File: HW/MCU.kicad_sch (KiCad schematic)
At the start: 7 parts, among them U6 STM32C031KxTx, U7 STM32C031KxUx

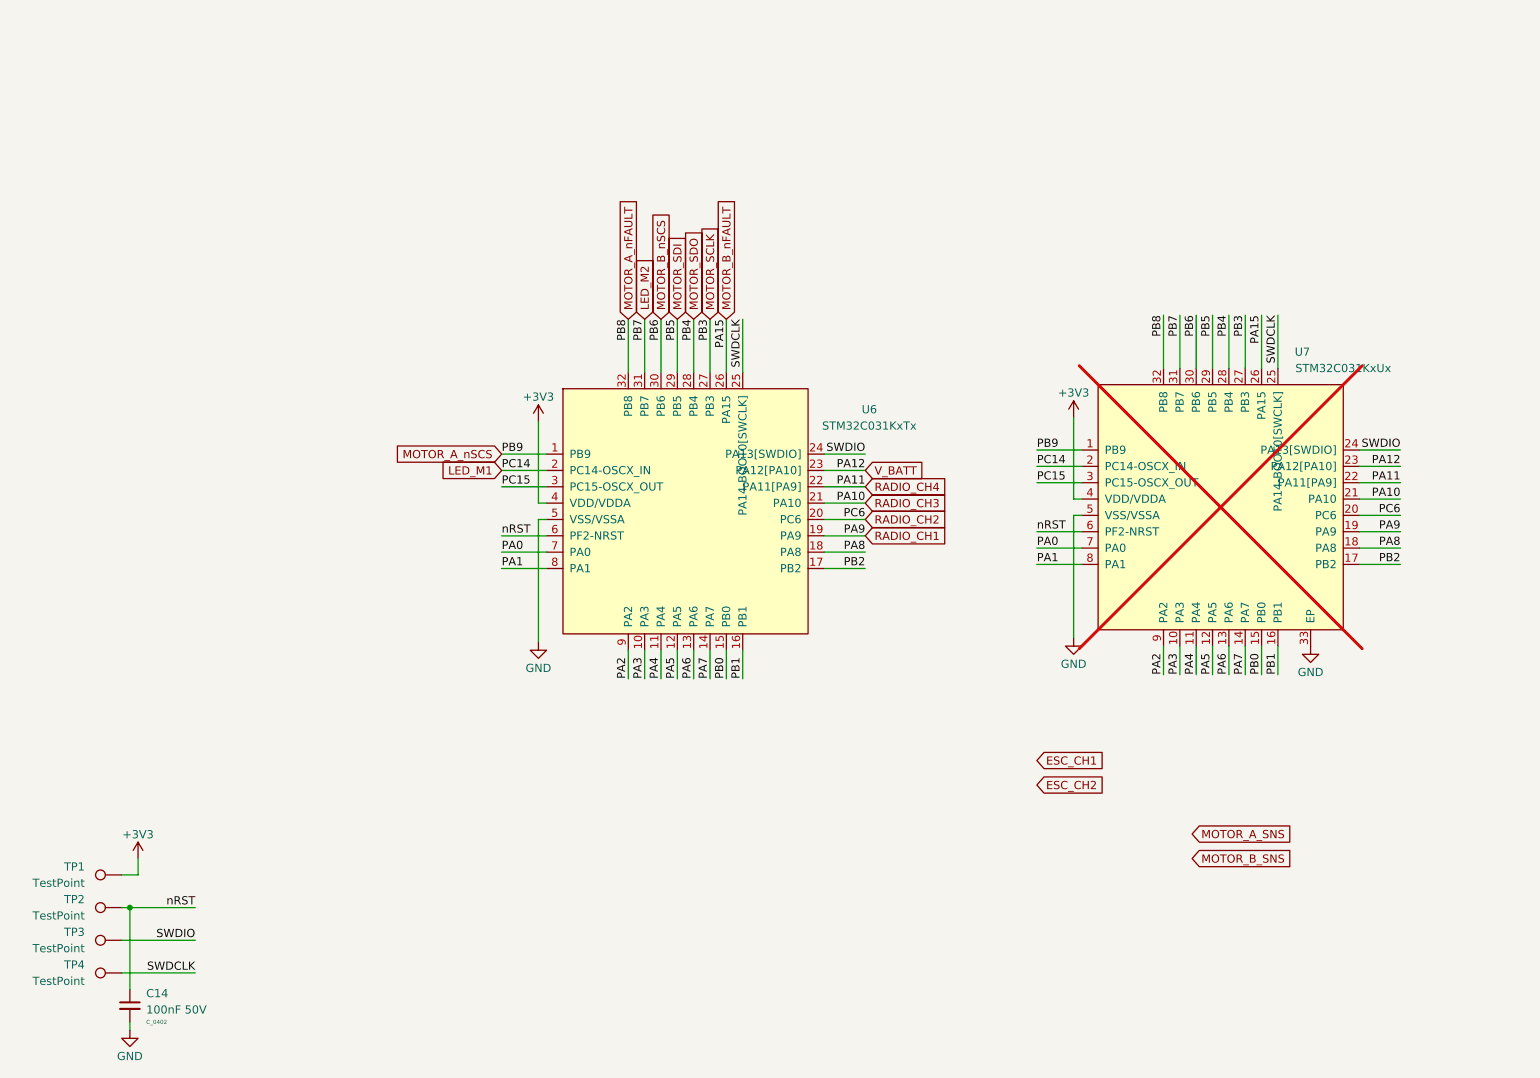
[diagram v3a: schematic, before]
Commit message: Move 5V Supply Around To Make More Efficient Conduction Path
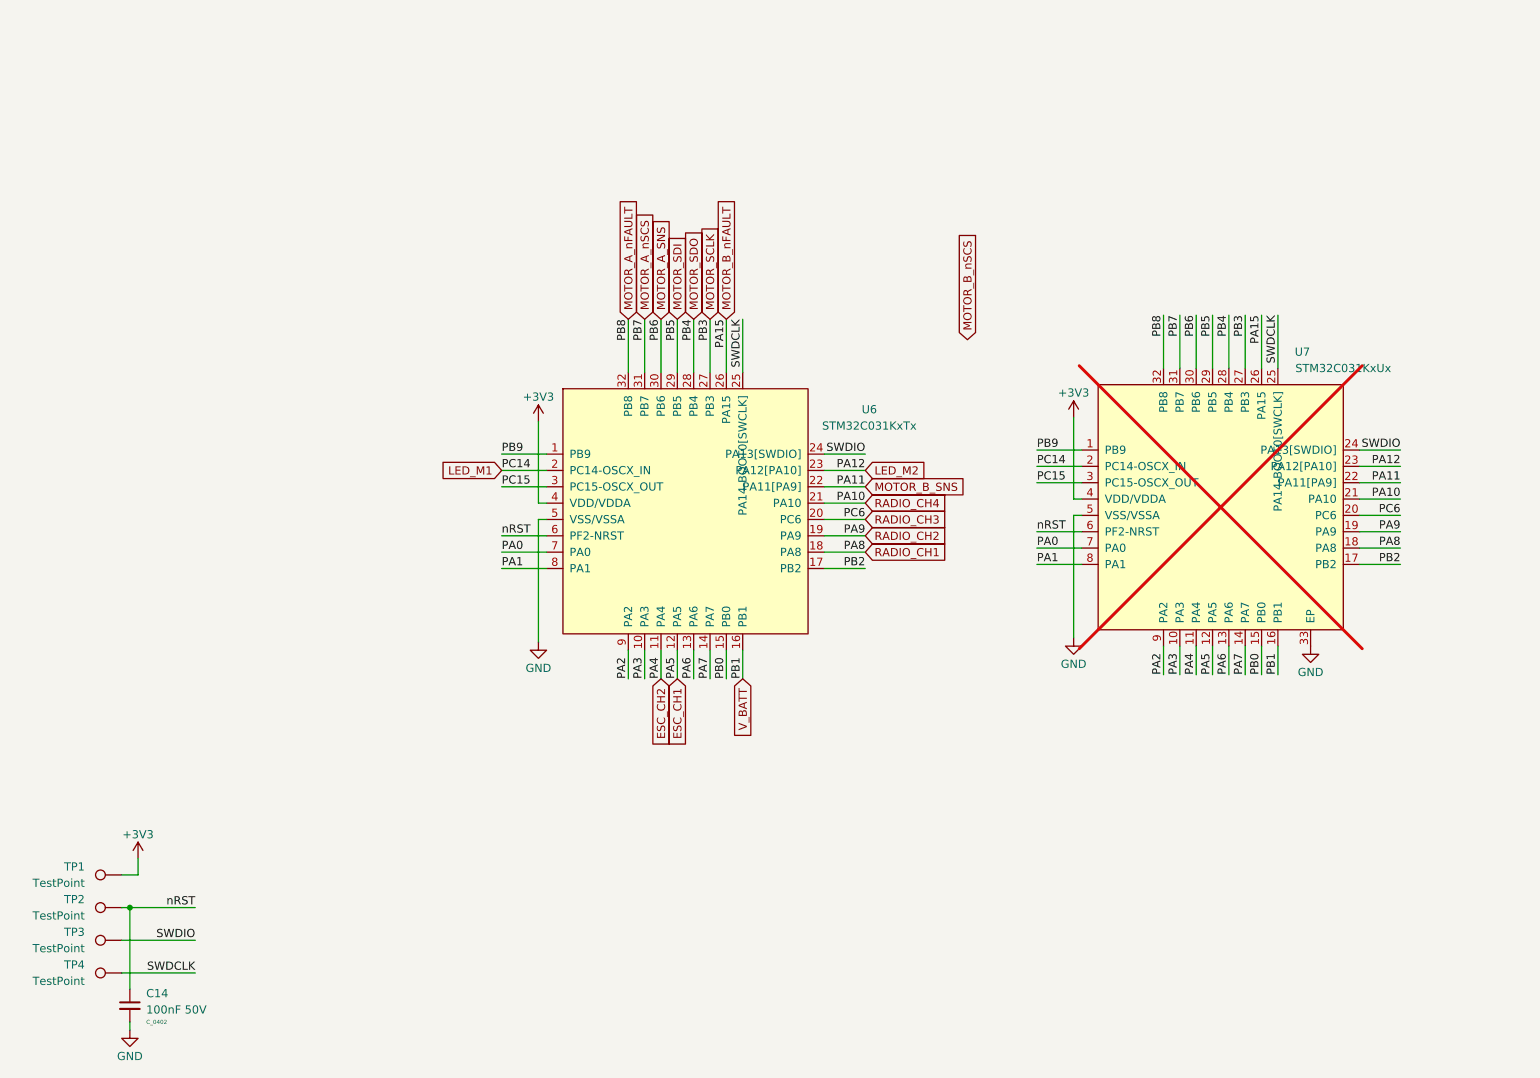
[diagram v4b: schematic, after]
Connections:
- net PA4 is gone; now on net ESC_CH2: U6.11 (PA4), U7.11 (PA4)
- net PA5 is gone; now on net ESC_CH1: U6.12 (PA5), U7.12 (PA5)
- net PA8 is gone; now on net RADIO_CH1: U6.18 (PA8), U7.18 (PA8)
- net PB1 is gone; now on net V_BATT: U6.16 (PB1), U7.16 (PB1)
- net LED_M2: now also U6.23 (PA12[PA10]), U7.23 (PA12[PA10]); no longer U6.31 (PB7), U7.31 (PB7)
- net MOTOR_A_SNS: now also U6.30 (PB6), U7.30 (PB6)
- net MOTOR_A_nSCS: now also U6.31 (PB7), U7.31 (PB7); no longer U6.1 (PB9), U7.1 (PB9)
- net MOTOR_B_SNS: now also U6.22 (PA11[PA9]), U7.22 (PA11[PA9])
- net MOTOR_B_nSCS: no longer U6.30 (PB6), U7.30 (PB6)
- net RADIO_CH1: no longer U6.19 (PA9), U7.19 (PA9)
- net RADIO_CH2: now also U6.19 (PA9), U7.19 (PA9); no longer U6.20 (PC6), U7.20 (PC6)
- net RADIO_CH3: now also U6.20 (PC6), U7.20 (PC6); no longer U6.21 (PA10), U7.21 (PA10)
- net RADIO_CH4: now also U6.21 (PA10), U7.21 (PA10); no longer U6.22 (PA11[PA9]), U7.22 (PA11[PA9])
- net V_BATT: no longer U6.23 (PA12[PA10]), U7.23 (PA12[PA10])
- new net PB9: U6.1 (PB9), U7.1 (PB9)
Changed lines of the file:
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@@
     (stroke (width 0) (type default))
   )
-  (wire (pts (xy 133.35 79.375) (xy 133.35 71.12))
+  (wire (pts (xy 133.35 71.12) (xy 133.35 79.375))
     (stroke (width 0) (type default))
   )
@@
     (effects (font (size 1.27 1.27)) (justify left bottom))
   )
-  (global_label "RADIO_CH2" (shape input) (at 167.64 102.235 0) (fields_autoplaced)
+  (global_label "V_BATT" (shape input) (at 148.59 127 270) (fields_autoplaced)
+    (effects (font (size 1.27 1.27)) (justify right))
+    (property "Intersheetrefs" "${INTERSHEET_REFS}" (at 148.59 136.3352 90)
+      (effects (font (size 1.27 1.27)) (justify right))
+    )
+  )
+  (global_label "MOTOR_A_SNS" (shape input) (at 135.89 71.12 90) (fields_autoplaced)
+    (effects (font (size 1.27 1.27)) (justify left))
+    (property "Intersheetrefs" "${INTERSHEET_REFS}" (at 135.89 55.0115 90)
+      (effects (font (size 1.27 1.27)) (justify left))
+    )
+  )
+  (global_label "RADIO_CH3" (shape input) (at 167.64 102.235 0) (fields_autoplaced)
     (effects (font (size 1.27 1.27)) (justify left))
     (property "Intersheetrefs" "${INTERSHEET_REFS}" (at 180.9667 102.235 0)
@@
     )
   )
-  (global_label "MOTOR_B_nSCS" (shape input) (at 135.89 71.12 90) (fields_autoplaced)
+  (global_label "ESC_CH2" (shape input) (at 135.89 127 270) (fields_autoplaced)
+    (effects (font (size 1.27 1.27)) (justify right))
+    (property "Intersheetrefs" "${INTERSHEET_REFS}" (at 135.89 138.3913 90)
+      (effects (font (size 1.27 1.27)) (justify right))
+    )
+  )
+  (global_label "MOTOR_A_nSCS" (shape input) (at 133.35 71.12 90) (fields_autoplaced)
     (effects (font (size 1.27 1.27)) (justify left))
-    (property "Intersheetrefs" "${INTERSHEET_REFS}" (at 135.89 53.7416 90)
+    (property "Intersheetrefs" "${INTERSHEET_REFS}" (at 133.35 53.923 90)
       (effects (font (size 1.27 1.27)) (justify left))
-    )
-  )
-  (global_label "V_BATT" (shape input) (at 167.64 94.615 0) (fields_autoplaced)
-    (effects (font (size 1.27 1.27)) (justify left))
-    (property "Intersheetrefs" "${INTERSHEET_REFS}" (at 176.9752 94.615 0)
-      (effects (font (size 1.27 1.27)) (justify left))
-    )
-  )
-  (global_label "ESC_CH2" (shape input) (at 194.31 143.51 0) (fields_autoplaced)
-    (effects (font (size 1.27 1.27)) (justify left))
-    (property "Intersheetrefs" "${INTERSHEET_REFS}" (at 205.7013 143.51 0)
-      (effects (font (size 1.27 1.27)) (justify left))
-    )
-  )
-  (global_label "RADIO_CH1" (shape input) (at 167.64 104.775 0) (fields_autoplaced)
-    (effects (font (size 1.27 1.27)) (justify left))
-    (property "Intersheetrefs" "${INTERSHEET_REFS}" (at 180.9667 104.775 0)
-      (effects (font (size 1.27 1.27)) (justify left))
-    )
-  )
-  (global_label "MOTOR_A_nSCS" (shape input) (at 111.125 92.075 180) (fields_autoplaced)
-    (effects (font (size 1.27 1.27)) (justify right))
-    (property "Intersheetrefs" "${INTERSHEET_REFS}" (at 93.928 92.075 0)
-      (effects (font (size 1.27 1.27)) (justify right))
     )
   )
@@
     )
   )
-  (global_label "ESC_CH1" (shape input) (at 194.31 139.7 0) (fields_autoplaced)
+  (global_label "MOTOR_B_nSCS" (shape input) (at 183.515 74.295 90) (fields_autoplaced)
     (effects (font (size 1.27 1.27)) (justify left))
-    (property "Intersheetrefs" "${INTERSHEET_REFS}" (at 205.7013 139.7 0)
+    (property "Intersheetrefs" "${INTERSHEET_REFS}" (at 183.515 56.9166 90)
       (effects (font (size 1.27 1.27)) (justify left))
     )
   )
-  (global_label "MOTOR_A_SNS" (shape input) (at 218.44 151.13 0) (fields_autoplaced)
-    (effects (font (size 1.27 1.27)) (justify left))
-    (property "Intersheetrefs" "${INTERSHEET_REFS}" (at 234.5485 151.13 0)
-      (effects (font (size 1.27 1.27)) (justify left))
+  (global_label "ESC_CH1" (shape input) (at 138.43 127 270) (fields_autoplaced)
+    (effects (font (size 1.27 1.27)) (justify right))
+    (property "Intersheetrefs" "${INTERSHEET_REFS}" (at 138.43 138.3913 90)
+      (effects (font (size 1.27 1.27)) (justify right))
     )
   )
@@
     )
   )
-  (global_label "RADIO_CH3" (shape input) (at 167.64 99.695 0) (fields_autoplaced)
+  (global_label "LED_M2" (shape input) (at 167.64 94.615 0) (fields_autoplaced)
     (effects (font (size 1.27 1.27)) (justify left))
-    (property "Intersheetrefs" "${INTERSHEET_REFS}" (at 180.9667 99.695 0)
+    (property "Intersheetrefs" "${INTERSHEET_REFS}" (at 177.7008 94.615 0)
       (effects (font (size 1.27 1.27)) (justify left))
     )
@@
     )
   )
-  (global_label "LED_M2" (shape input) (at 133.35 71.12 90) (fields_autoplaced)
+  (global_label "RADIO_CH4" (shape input) (at 167.64 99.695 0) (fields_autoplaced)
     (effects (font (size 1.27 1.27)) (justify left))
-    (property "Intersheetrefs" "${INTERSHEET_REFS}" (at 133.35 61.0592 90)
+    (property "Intersheetrefs" "${INTERSHEET_REFS}" (at 180.9667 99.695 0)
+      (effects (font (size 1.27 1.27)) (justify left))
+    )
+  )
+  (global_label "MOTOR_B_SNS" (shape input) (at 167.64 97.155 0) (fields_autoplaced)
+    (effects (font (size 1.27 1.27)) (justify left))
+    (property "Intersheetrefs" "${INTERSHEET_REFS}" (at 183.9299 97.155 0)
+      (effects (font (size 1.27 1.27)) (justify left))
+    )
+  )
+  (global_label "RADIO_CH1" (shape input) (at 167.64 107.315 0) (fields_autoplaced)
+    (effects (font (size 1.27 1.27)) (justify left))
+    (property "Intersheetrefs" "${INTERSHEET_REFS}" (at 180.9667 107.315 0)
       (effects (font (size 1.27 1.27)) (justify left))
     )
@@
     )
   )
-  (global_label "RADIO_CH4" (shape input) (at 167.64 97.155 0) (fields_autoplaced)
+  (global_label "RADIO_CH2" (shape input) (at 167.64 104.775 0) (fields_autoplaced)
     (effects (font (size 1.27 1.27)) (justify left))
-    (property "Intersheetrefs" "${INTERSHEET_REFS}" (at 180.9667 97.155 0)
+    (property "Intersheetrefs" "${INTERSHEET_REFS}" (at 180.9667 104.775 0)
       (effects (font (size 1.27 1.27)) (justify left))
     )
-  )
-  (global_label "MOTOR_B_SNS" (shape input) (at 218.44 154.94 0) (fields_autoplaced)
-    (effects (font (size 1.27 1.27)) (justify left))
-    (property "Intersheetrefs" "${INTERSHEET_REFS}" (at 234.7299 154.94 0)
-      (effects (font (size 1.27 1.27)) (justify left))
-    )

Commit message: Finish Tracking and Release For MFG
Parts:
- removed TP1: TestPoint, TestPoint:TestPoint_Pad_D1.5mm, symbol Connector:TestPoint
- added C40: 100nF 50V, C_Capacitor:C_0402, symbol C_Capacitor:C_0402
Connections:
- net PA0 is gone; now on net LED_M1: U6.7 (PA0), U7.7 (PA0)
- net PA1 is gone; now on net V_BATT: U6.8 (PA1), U7.8 (PA1)
- net PB0 is gone; now on net LED_M2: U6.15 (PB0), U7.15 (PB0)
- net PB2 is gone; now on net ESC_CH2: U6.17 (PB2), U7.17 (PB2)
- net PB9 is gone; now on net MOTOR_A_nSCS: U6.1 (PB9), U7.1 (PB9)
- net +3V3: now also C40.1
- net ESC_CH1: now also U6.16 (PB1), U7.16 (PB1); no longer U6.12 (PA5), U7.12 (PA5)
- net ESC_CH2: no longer U6.11 (PA4), U7.11 (PA4)
- net GND: now also C40.2
- net LED_M1: no longer U6.2 (PC14-OSCX_IN), U7.2 (PC14-OSCX_IN)
- net LED_M2: no longer U6.23 (PA12[PA10]), U7.23 (PA12[PA10])
- net MOTOR_A_SNS: now also U6.22 (PA11[PA9]), U7.22 (PA11[PA9]); no longer U6.30 (PB6), U7.30 (PB6)
- net MOTOR_A_nFAULT: now also U6.31 (PB7), U7.31 (PB7); no longer U6.32 (PB8), U7.32 (PB8)
- net MOTOR_A_nSCS: no longer U6.31 (PB7), U7.31 (PB7)
- net MOTOR_B_SNS: now also U6.23 (PA12[PA10]), U7.23 (PA12[PA10]); no longer U6.22 (PA11[PA9]), U7.22 (PA11[PA9])
- net MOTOR_B_nFAULT: now also U6.30 (PB6), U7.30 (PB6); no longer U6.26 (PA15), U7.26 (PA15)
- net MOTOR_B_nSCS: now also U6.26 (PA15), U7.26 (PA15)
- net V_BATT: no longer U6.16 (PB1), U7.16 (PB1)
- new net PA4: U6.11 (PA4), U7.11 (PA4)
- new net PA5: U6.12 (PA5), U7.12 (PA5)
- new net PB8: U6.32 (PB8), U7.32 (PB8)
- new net PC14: U6.2 (PC14-OSCX_IN), U7.2 (PC14-OSCX_IN)
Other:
- title: KAKAPO ESC - 20A -> KAKAPO - 20A

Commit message: Create v1.0 Fixed From v0.2 HW
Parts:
- TP2, TP3, TP4: now left out of the parts list
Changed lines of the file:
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@@
   )
   (symbol (lib_id "Connector:TestPoint") (at 52.07 172.72 90) (mirror x) (unit 1)
-    (in_bom yes) (on_board yes) (dnp no) (fields_autoplaced)
+    (in_bom no) (on_board yes) (dnp no) (fields_autoplaced)
     (property "Reference" "TP4" (at 46.3296 171.4499 90)
       (effects (font (size 1.27 1.27)) (justify left))
@@
   )
   (symbol (lib_id "Connector:TestPoint") (at 52.07 167.64 90) (mirror x) (unit 1)
-    (in_bom yes) (on_board yes) (dnp no) (fields_autoplaced)
+    (in_bom no) (on_board yes) (dnp no) (fields_autoplaced)
     (property "Reference" "TP3" (at 46.3296 166.3699 90)
       (effects (font (size 1.27 1.27)) (justify left))
@@
   )
   (symbol (lib_id "Connector:TestPoint") (at 52.07 162.56 90) (mirror x) (unit 1)
-    (in_bom yes) (on_board yes) (dnp no) (fields_autoplaced)
+    (in_bom no) (on_board yes) (dnp no) (fields_autoplaced)
     (property "Reference" "TP2" (at 46.3296 161.2899 90)
       (effects (font (size 1.27 1.27)) (justify left))
